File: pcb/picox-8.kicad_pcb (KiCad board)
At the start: 2 copper layers, 287.5 x 119 mm, 86 parts, among them J1 PX-8 Expansion Port, U1 XC95144XL-TQ100

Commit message: PCB work
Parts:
- added J2: Mini-DIN-8, Connector_DIN:minidin-8, F.Cu at (247.7, 96.0)
- added J3: SD_Card, Connector_Card:SD_TE_2041021, F.Cu at (286.5, 102.5)
- added SW1: SW_Push, Button_Switch_THT:SW_Tactile_SPST_Angled_PTS645Vx39-2LFS, F.Cu at (260.2, 92.0)
- added U2: MAX3232, Package_SO:SOP-16_3.9x9.9mm_P1.27mm, F.Cu at (229.3, 112.0)
- added U3: Pico_W, RPI PIco:RPi_Pico_SMD_TH, F.Cu at (205.1, 175.1)
- added U4: AZ1117-3.3, Package_TO_SOT_SMD:SOT-223, F.Cu at (232.3, 163.2)
- moved R4 64.1 mm to (122.0, 117.7)
- moved R1 62.6 mm to (123.6, 114.2)
- moved R10 62.6 mm to (128.1, 117.7)
- moved R12 62.6 mm to (129.6, 117.7)
- moved R13 62.6 mm to (131.2, 114.2)
- moved R14 62.6 mm to (131.2, 117.7)
- moved R15 62.6 mm to (132.7, 114.2)
- moved R17 62.6 mm to (134.2, 114.2)
- moved R18 62.6 mm to (134.2, 117.7)
- moved R19 62.6 mm to (135.7, 114.2)
- moved R20 62.6 mm to (135.7, 117.7)
- moved R21 62.6 mm to (137.3, 114.2)
- moved R23 62.6 mm to (138.8, 114.2)
- moved R25 62.6 mm to (140.3, 114.2)
- moved R27 62.6 mm to (141.8, 114.2)
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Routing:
- net /A11: track 64.7 -> 0.00 mm
- net /A13: track 63.2 -> 0.00 mm
- net GND: track 0.00 -> 62.8 mm, vias 0 -> 42
- net /A12: track 62.4 -> 0.00 mm
- net /A2: track 61.7 -> 0.00 mm
- net /A14: track 60.9 -> 0.00 mm
- net /A0: track 60.3 -> 0.00 mm
- net /A1: track 59.4 -> 0.00 mm
- net /A3: track 58.7 -> 0.00 mm
- net /A15: track 57.9 -> 0.00 mm
- net /A4: track 56.5 -> 0.00 mm
- net /A5: track 56.1 -> 0.00 mm
- net /A6: track 54.4 -> 0.00 mm
- net /A7: track 53.3 -> 0.00 mm
- net /A10: track 51.5 -> 0.00 mm
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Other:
- outline, holes or cut-outs redrawn

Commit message: pcb work
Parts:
- removed U4: AZ1117-3.3, Package_TO_SOT_SMD:SOT-223
- added C1: 100nF, Capacitor_SMD:C_0603_1608Metric_Pad1.08x0.95mm_HandSolder, B.Cu at (158.4, 143.1)
- added C2: 100nF, Capacitor_SMD:C_0603_1608Metric_Pad1.08x0.95mm_HandSolder, B.Cu at (161.4, 143.1)
- added C3: 100nF, Capacitor_SMD:C_0603_1608Metric_Pad1.08x0.95mm_HandSolder, B.Cu at (160.4, 148.3)
- added C4: 100nF, Capacitor_SMD:C_0603_1608Metric_Pad1.08x0.95mm_HandSolder, B.Cu at (160.4, 154.4)
- added C5: 100nF, Capacitor_SMD:C_0603_1608Metric_Pad1.08x0.95mm_HandSolder, B.Cu at (150.1, 148.3)
- added C6: 100nF, Capacitor_SMD:C_0603_1608Metric_Pad1.08x0.95mm_HandSolder, B.Cu at (150.4, 153.3)
- added C7: 100nF, Capacitor_SMD:C_0603_1608Metric_Pad1.08x0.95mm_HandSolder, B.Cu at (151.4, 158.6)
- added J4: USB_C_Receptacle_USB2.0, Connector_USB:USB_C_Receptacle_G-Switch_GT-USB-7010ASV, F.Cu at (326.6, 93.1)
- added J5: CONN_CPLD_JTAG, Connector_IDC:IDC-Header_2x05_P2.54mm_Vertical, F.Cu at (95.6, 118.7)
- added Q1: Q_PMOS_DGS, Package_TO_SOT_SMD:SOT-23-3, F.Cu at (234.5, 124.4)
- added U5: MCP73871-2CC, Package_DFN_QFN:QFN-20-1EP_4x4mm_P0.5mm_EP2.5x2.5mm, F.Cu at (246.3, 177.3)
- J3: value SD_Card -> 693063010911; footprint Connector_Card:SD_TE_2041021 -> hans-kicad-footprints:Wuerth SD Card 693063010911
- moved U3 30.2 mm to (216.3, 147.0)
- moved U2 18.6 mm to (247.9, 111.6), turned to 90 degrees
- moved J3 3.58 mm to (283.0, 102.1)
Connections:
- J2 pad 10: (no net) -> unconnected-(J2-SHIELD-Pad10)
- J2 pad 11: (no net) -> unconnected-(J2-SHIELD-Pad11)
- J2 pad 9: (no net) -> unconnected-(J2-SHIELD-Pad9)
- J3 pad 1: unconnected-(J3-CD/DAT3-Pad1) -> /SD_CS
- J3 pad 10: unconnected-(J3-CARD_DETECT-Pad10) -> /SD_CD
- J3 pad 11: unconnected-(J3-WRITE_PROTECT-Pad11) -> /SD_WP
- J3 pad 2: unconnected-(J3-CMD-Pad2) -> /SD_MOSI
- J3 pad 3: unconnected-(J3-VSS-Pad3) -> GND
- J3 pad 4: unconnected-(J3-VDD-Pad4) -> +3.3V
- J3 pad 5: unconnected-(J3-CLK-Pad5) -> /SD_CLK
- J3 pad 6: unconnected-(J3-VSS-Pad6) -> GND
- J3 pad 7: unconnected-(J3-DAT0-Pad7) -> /SD_MISO
- SW1 pad 1: unconnected-(SW1-Pad1) -> /BTN_FAILSAFE
- SW1 pad 2: unconnected-(SW1-Pad2) -> GND
- U1 pad 100: unconnected-(U1-GND-Pad100) -> GND
- U1 pad 21: unconnected-(U1-GND-Pad21) -> GND
- U1 pad 26: unconnected-(U1-VCCIO-Pad26) -> +3.3V
- U1 pad 31: unconnected-(U1-GND-Pad31) -> GND
- U1 pad 38: unconnected-(U1-VCCIO-Pad38) -> +3.3V
- U1 pad 44: unconnected-(U1-GND-Pad44) -> GND
- U1 pad 45: unconnected-(U1-TDI-Pad45) -> Net-(J5-TDI)
- U1 pad 47: unconnected-(U1-TMS-Pad47) -> Net-(J5-TMS)
- U1 pad 48: unconnected-(U1-TCK-Pad48) -> Net-(J5-TCK)
- U1 pad 5: unconnected-(U1-VCCINT-Pad5) -> +3.3V
- U1 pad 51: unconnected-(U1-VCCIO-Pad51) -> +3.3V
- U1 pad 57: unconnected-(U1-VCCINT-Pad57) -> +3.3V
- U1 pad 62: unconnected-(U1-GND-Pad62) -> GND
- U1 pad 69: unconnected-(U1-GND-Pad69) -> GND
- U1 pad 75: unconnected-(U1-GND-Pad75) -> GND
- U1 pad 83: unconnected-(U1-TDO-Pad83) -> Net-(J5-TDO)
- U1 pad 84: unconnected-(U1-GND-Pad84) -> GND
- U1 pad 88: unconnected-(U1-VCCIO-Pad88) -> +3.3V
- U1 pad 98: unconnected-(U1-VCCINT-Pad98) -> +3.3V
- U3 pad 21: unconnected-(U3-GPIO16-Pad21) -> /SD_MISO
- U3 pad 22: unconnected-(U3-GPIO17-Pad22) -> /SD_CS
- U3 pad 24: unconnected-(U3-GPIO18-Pad24) -> /SD_CLK
- U3 pad 25: unconnected-(U3-GPIO19-Pad25) -> /SD_MOSI
- U3 pad 26: unconnected-(U3-GPIO20-Pad26) -> /SD_CD
- U3 pad 27: unconnected-(U3-GPIO21-Pad27) -> /SD_WP
- U3 pad 29: unconnected-(U3-GPIO22-Pad29) -> /BTN_FAILSAFE
- U3 pad 39: unconnected-(U3-VSYS-Pad39) -> /VSYS
- U3 pad 40: unconnected-(U3-VBUS-Pad40) -> /VBUS
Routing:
- net +3.3V: track 0.00 -> 11.7 mm, vias 0 -> 7
- added copper zone on B.Cu, net GND
- added copper zone on F.Cu, net GND

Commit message: cpld & pcb work
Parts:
- added C10: 100nF, Capacitor_SMD:C_0603_1608Metric_Pad1.08x0.95mm_HandSolder, F.Cu at (253.2, 113.5)
- added C11: 100nF, Capacitor_SMD:C_0603_1608Metric_Pad1.08x0.95mm_HandSolder, F.Cu at (253.2, 109.0)
- added C12: 100nF, Capacitor_SMD:C_0603_1608Metric_Pad1.08x0.95mm_HandSolder, F.Cu at (241.7, 113.3)
- added C8: 100nF, Capacitor_SMD:C_0603_1608Metric_Pad1.08x0.95mm_HandSolder, F.Cu at (253.2, 112.0)
- added C9: 100nF, Capacitor_SMD:C_0603_1608Metric_Pad1.08x0.95mm_HandSolder, F.Cu at (253.2, 110.5)
- added R85: 10k, Resistor_SMD:R_0603_1608Metric_Pad0.98x0.95mm_HandSolder, F.Cu at (231.4, 139.0)
- added R86: 10k, Resistor_SMD:R_0603_1608Metric_Pad0.98x0.95mm_HandSolder, F.Cu at (231.4, 142.5)
- added SW2: RESET, Button_Switch_THT:SW_Tactile_SPST_Angled_PTS645Vx39-2LFS, F.Cu at (317.6, 92.0)
- J2: value Mini-DIN-8 -> SERIAL
- SW1: value SW_Push -> FAILSAFE
- U2: value MAX3232 -> MAX3222; footprint Package_SO:SOP-16_3.9x9.9mm_P1.27mm -> Package_SO:TSSOP-20_4.4x5mm_P0.5mm
- U3: footprint RPI PIco:RPi_Pico_SMD_TH -> RPI PIco:RPI Pico W USB and Prog
- moved J4 50.4 mm to (276.2, 93.1)
- moved J3 16.7 mm to (299.7, 102.3)
- moved Q1 2.64 mm to (231.9, 124.4)
- moved U2 0.41 mm to (247.4, 111.6), turned to 180 degrees
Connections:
- net /VSYS renamed /PICO_VSYS
- J2 pad 1: unconnected-(J2-Pad1) -> GND
- J2 pad 10: unconnected-(J2-SHIELD-Pad10) -> GND
- J2 pad 11: unconnected-(J2-SHIELD-Pad11) -> GND
- J2 pad 2: unconnected-(J2-Pad2) -> Net-(U2-R1IN)
- J2 pad 3: unconnected-(J2-Pad3) -> Net-(U2-T1OUT)
- J2 pad 6: unconnected-(J2-Pad6) -> Net-(U2-T2OUT)
- J2 pad 7: unconnected-(J2-Pad7) -> Net-(U2-R2IN)
- J2 pad 9: unconnected-(J2-SHIELD-Pad9) -> GND
- J4 pad A1: Net-(J4-GND-PadA1) -> GND
- J4 pad A12: Net-(J4-GND-PadA1) -> GND
- J4 pad A4: Net-(J4-VBUS-PadA4) -> /VBUS
- J4 pad A9: Net-(J4-VBUS-PadA4) -> /VBUS
- J4 pad B1: Net-(J4-GND-PadA1) -> GND
- J4 pad B12: Net-(J4-GND-PadA1) -> GND
- J4 pad B4: Net-(J4-VBUS-PadA4) -> /VBUS
- J4 pad B9: Net-(J4-VBUS-PadA4) -> /VBUS
- J4 pad S1: unconnected-(J4-SHIELD-PadS1) -> GND
- Q1 pad 1: Net-(Q1-D) -> /VB1
- Q1 pad 2: /VBUS -> /PICO_VBUS
- U1 pad 10: unconnected-(U1-P10-Pad10) -> /SER_HSOUT
- U1 pad 11: unconnected-(U1-P11-Pad11) -> /SER_HSIN
- U1 pad 12: unconnected-(U1-P12-Pad12) -> /PICO_A2
- U1 pad 13: unconnected-(U1-P13-Pad13) -> /PICO_A1
- U1 pad 14: unconnected-(U1-P14-Pad14) -> /PICO_A0
- U1 pad 15: unconnected-(U1-P15-Pad15) -> /PICO_STB
- U1 pad 16: unconnected-(U1-P16-Pad16) -> /PICO_DIR
- U1 pad 17: unconnected-(U1-P17-Pad17) -> /PICO_CLK
- U1 pad 18: unconnected-(U1-P18-Pad18) -> /PICO_D7
- U1 pad 19: unconnected-(U1-P19-Pad19) -> /PICO_D6
- U1 pad 20: unconnected-(U1-P20-Pad20) -> /PICO_D5
- U1 pad 24: unconnected-(U1-P24-Pad24) -> /PICO_D4
- U1 pad 25: unconnected-(U1-P25-Pad25) -> /PICO_D3
- U1 pad 28: unconnected-(U1-P28-Pad28) -> /PICO_D2
- U1 pad 29: unconnected-(U1-P29-Pad29) -> /PICO_D1
- U1 pad 30: unconnected-(U1-P30-Pad30) -> /PICO_D0
- U1 pad 32: unconnected-(U1-P32-Pad32) -> /PICO_RXD0
- U1 pad 33: unconnected-(U1-P33-Pad33) -> /PICO_TXD0
- U1 pad 8: unconnected-(U1-P8-Pad8) -> /~{SER_EN}
- U1 pad 87: unconnected-(U1-P87-Pad87) -> /SD_WP
- U1 pad 89: unconnected-(U1-P89-Pad89) -> /SD_CD
- U1 pad 9: unconnected-(U1-P9-Pad9) -> /~{SER_SHDN}
- U1 pad 90: unconnected-(U1-P90-Pad90) -> /BTN_FAILSAFE
- U1 pad 91: unconnected-(U1-P91-Pad91) -> /BTN_RESET
- U2 pad 1: unconnected-(U2-C1+-Pad1) -> /~{SER_EN}
- U2 pad 10: unconnected-(U2-T2IN-Pad10) -> /SER_HSIN
- U2 pad 12: unconnected-(U2-R1OUT-Pad12) -> /SER_HSOUT
- U2 pad 13: unconnected-(U2-R1IN-Pad13) -> /PICO_TXD1
- U2 pad 15: unconnected-(U2-GND-Pad15) -> /PICO_RXD1
- U2 pad 16: unconnected-(U2-VCC-Pad16) -> Net-(U2-R1IN)
- U2 pad 2: unconnected-(U2-VS+-Pad2) -> Net-(U2-C1+)
- U2 pad 3: unconnected-(U2-C1--Pad3) -> Net-(U2-VS+)
- U2 pad 4: unconnected-(U2-C2+-Pad4) -> Net-(U2-C1-)
- U2 pad 5: unconnected-(U2-C2--Pad5) -> Net-(U2-C2+)
- U2 pad 6: unconnected-(U2-VS--Pad6) -> Net-(U2-C2-)
- U2 pad 7: unconnected-(U2-T2OUT-Pad7) -> Net-(U2-VS-)
- U2 pad 8: unconnected-(U2-R2IN-Pad8) -> Net-(U2-T2OUT)
- U2 pad 9: unconnected-(U2-R2OUT-Pad9) -> Net-(U2-R2IN)
- U3 pad 1: unconnected-(U3-GPIO0-Pad1) -> /PICO_TXD0
- U3 pad 10: unconnected-(U3-GPIO7-Pad10) -> /PICO_D5
- U3 pad 11: unconnected-(U3-GPIO8-Pad11) -> /PICO_D6
- U3 pad 12: unconnected-(U3-GPIO9-Pad12) -> /PICO_D7
- U3 pad 13: unconnected-(U3-GND-Pad13) -> GND
- U3 pad 14: unconnected-(U3-GPIO10-Pad14) -> /PICO_CLK
- U3 pad 15: unconnected-(U3-GPIO11-Pad15) -> /PICO_DIR
- U3 pad 16: unconnected-(U3-GPIO12-Pad16) -> /PICO_STB
- U3 pad 17: unconnected-(U3-GPIO13-Pad17) -> /PICO_A0
- U3 pad 18: unconnected-(U3-GND-Pad18) -> GND
- U3 pad 19: unconnected-(U3-GPIO14-Pad19) -> /PICO_A1
- U3 pad 2: unconnected-(U3-GPIO1-Pad2) -> /PICO_RXD0
- U3 pad 20: unconnected-(U3-GPIO15-Pad20) -> /PICO_A2
- U3 pad 23: unconnected-(U3-GND-Pad23) -> GND
- U3 pad 26: /SD_CD -> /PICO_TXD1
- U3 pad 27: /SD_WP -> /PICO_RXD1
- U3 pad 28: unconnected-(U3-GND-Pad28) -> GND
- U3 pad 29: /BTN_FAILSAFE -> unconnected-(U3-GPIO22-Pad29)
- U3 pad 3: unconnected-(U3-GND-Pad3) -> GND
- U3 pad 33: unconnected-(U3-AGND-Pad33) -> GND
- U3 pad 34: unconnected-(U3-GPIO28_ADC2-Pad34) -> Net-(U3-GPIO28_ADC2)
- U3 pad 35: unconnected-(U3-ADC_VREF-Pad35) -> +3.3V
- U3 pad 36: unconnected-(U3-3V3-Pad36) -> +3.3V
- U3 pad 38: unconnected-(U3-GND-Pad38) -> GND
- U3 pad 4: unconnected-(U3-GPIO2-Pad4) -> /PICO_D0
- U3 pad 40: /VBUS -> /PICO_VBUS
- U3 pad 5: unconnected-(U3-GPIO3-Pad5) -> /PICO_D1
- U3 pad 6: unconnected-(U3-GPIO4-Pad6) -> /PICO_D2
- U3 pad 7: unconnected-(U3-GPIO5-Pad7) -> /PICO_D3
- U3 pad 8: unconnected-(U3-GND-Pad8) -> GND
- U3 pad 9: unconnected-(U3-GPIO6-Pad9) -> /PICO_D4
- U3 pad TP1: GND -> unconnected-(U3-USB_GND-PadTP1)
- U3 pad TP2: /USB_D- -> GND
- U3 pad TP3: /USB_D+ -> /USB_D-
- U5 pad 1: Net-(Q1-D) -> /VB1
- U5 pad 2: unconnected-(U5-VPCC-Pad2) -> /VBUS
- U5 pad 20: Net-(Q1-D) -> /VB1
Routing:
- net Net-(U2-T1OUT): track 0.00 -> 17.4 mm, vias 0 -> 1
- net Net-(U2-T2OUT): track 0.00 -> 14.4 mm, vias 0 -> 1
- net Net-(U2-R2IN): track 0.00 -> 14.3 mm
- net Net-(U2-R1IN): track 0.00 -> 12.4 mm
- net /PICO_VBUS: track 0.00 -> 8.02 mm
- net Net-(U3-GPIO28_ADC2): track 0.00 -> 6.18 mm
- net /PICO_VSYS: track 0.00 -> 6.00 mm
- net Net-(U2-C1+): track 0.00 -> 5.84 mm
- net Net-(U2-C2+): track 0.00 -> 4.35 mm
- net Net-(U2-VS-): track 0.00 -> 3.14 mm
- net Net-(U2-C2-): track 0.00 -> 2.42 mm
- net Net-(U2-VS+): track 0.00 -> 2.36 mm
- net Net-(U2-C1-): track 0.00 -> 2.20 mm
- net +3.3V: track 11.7 -> 13.8 mm
- net /SPI: track 0.00 -> 1.63 mm

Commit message: schematic nearing completion
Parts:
- added C13: 10μF, Capacitor_SMD:C_0603_1608Metric_Pad1.08x0.95mm_HandSolder, F.Cu at (261.0, 169.5)
- added C14: 4.7μF, Capacitor_SMD:C_0603_1608Metric_Pad1.08x0.95mm_HandSolder, F.Cu at (261.0, 172.0)
- added C15: 4.7μF, Capacitor_SMD:C_0603_1608Metric_Pad1.08x0.95mm_HandSolder, F.Cu at (261.0, 174.6)
- added J6: NTC, Connector_PinHeader_2.54mm:PinHeader_1x02_P2.54mm_Vertical, F.Cu at (247.8, 123.6)
- added J7: BAT, Connector_JST:JST_EH_S2B-EH_1x02_P2.50mm_Horizontal, F.Cu at (277.1, 167.1)
- added R87: 10k, Resistor_SMD:R_0603_1608Metric_Pad0.98x0.95mm_HandSolder, F.Cu at (261.0, 177.1)
- added R88: 10k, Resistor_SMD:R_0603_1608Metric_Pad0.98x0.95mm_HandSolder, F.Cu at (261.0, 179.6)
- added R89: 0, Resistor_SMD:R_0603_1608Metric_Pad0.98x0.95mm_HandSolder, F.Cu at (261.0, 182.1)
- added R90: DNP, Resistor_SMD:R_0603_1608Metric_Pad0.98x0.95mm_HandSolder, F.Cu at (261.0, 184.6)
- added R91: 1k, Resistor_SMD:R_0603_1608Metric_Pad0.98x0.95mm_HandSolder, F.Cu at (261.0, 187.1)
- added R92: 10k, Resistor_SMD:R_0603_1608Metric_Pad0.98x0.95mm_HandSolder, F.Cu at (261.0, 189.6)
- moved U5 32.0 mm to (278.3, 175.3), turned to 90 degrees
- moved Q1 22.8 mm to (213.9, 138.4)
- moved R85 22.8 mm to (213.4, 153.0)
- moved R86 22.8 mm to (213.4, 156.5)
- moved U3 22.8 mm to (198.4, 161.0)
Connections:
- U1 pad 1: unconnected-(U1-I/O/GTS3-Pad1) -> /CHG_~{TE}
- U1 pad 2: unconnected-(U1-I/O/GTS4-Pad2) -> /CHG_CE
- U1 pad 92: unconnected-(U1-P92-Pad92) -> /PICO_RESET
- U1 pad 93: unconnected-(U1-P93-Pad93) -> /PICO_BOOTSEL
- U1 pad 94: unconnected-(U1-P94-Pad94) -> /CHG_STAT1
- U1 pad 95: unconnected-(U1-P95-Pad95) -> /CHG_STAT2
- U1 pad 96: unconnected-(U1-P96-Pad96) -> /CHG_~{PG}
- U1 pad 97: unconnected-(U1-P97-Pad97) -> /CHG_SEL
- U1 pad 99: unconnected-(U1-I/O/GSR-Pad99) -> /CHG_PROG2
- U3 pad 30: unconnected-(U3-RUN-Pad30) -> /PICO_RUN
- U3 pad 31: unconnected-(U3-GPIO26_ADC0-Pad31) -> /PICO_SER_HSOUT
- U3 pad 32: unconnected-(U3-GPIO27_ADC1-Pad32) -> /PICO_SER_HSIN
- U3 pad TP1: unconnected-(U3-USB_GND-PadTP1) -> GND
- U3 pad TP2: GND -> /USB_D-
- U3 pad TP3: /USB_D- -> /USB_D+
- U3 pad TP6: /USB_D+ -> /PICO_BOOTSEL
- U5 pad 10: Net-(U5-V_{SS}-Pad10) -> GND
- U5 pad 11: Net-(U5-V_{SS}-Pad10) -> GND
- U5 pad 12: unconnected-(U5-PROG3-Pad12) -> Net-(U5-PROG3)
- U5 pad 13: unconnected-(U5-PROG1-Pad13) -> Net-(U5-PROG1)
- U5 pad 14: Net-(U5-V_{BAT}-Pad14) -> /VBAT
- U5 pad 15: Net-(U5-V_{BAT}-Pad14) -> /VBAT
- U5 pad 16: unconnected-(U5-V_{BAT_SENSE}-Pad16) -> /VBAT
- U5 pad 17: unconnected-(U5-CE-Pad17) -> /CHG_CE
- U5 pad 18: Net-(U5-IN-Pad18) -> /VBUS
- U5 pad 19: Net-(U5-IN-Pad18) -> /VBUS
- U5 pad 21: Net-(U5-V_{SS}-Pad10) -> GND
- U5 pad 3: unconnected-(U5-SEL-Pad3) -> /CHG_SEL
- U5 pad 4: unconnected-(U5-PROG2-Pad4) -> /CHG_PROG2
- U5 pad 5: unconnected-(U5-THERM-Pad5) -> Net-(U5-THERM)
- U5 pad 6: unconnected-(U5-~{PG}-Pad6) -> /CHG_~{PG}
- U5 pad 7: unconnected-(U5-STAT2-Pad7) -> /CHG_STAT2
- U5 pad 8: unconnected-(U5-STAT1/~{LBO}-Pad8) -> /CHG_STAT1
- U5 pad 9: unconnected-(U5-~{TE}-Pad9) -> /CHG_~{TE}
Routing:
- net /VBAT: track 0.00 -> 8.29 mm
- net GND: vias 42 -> 46

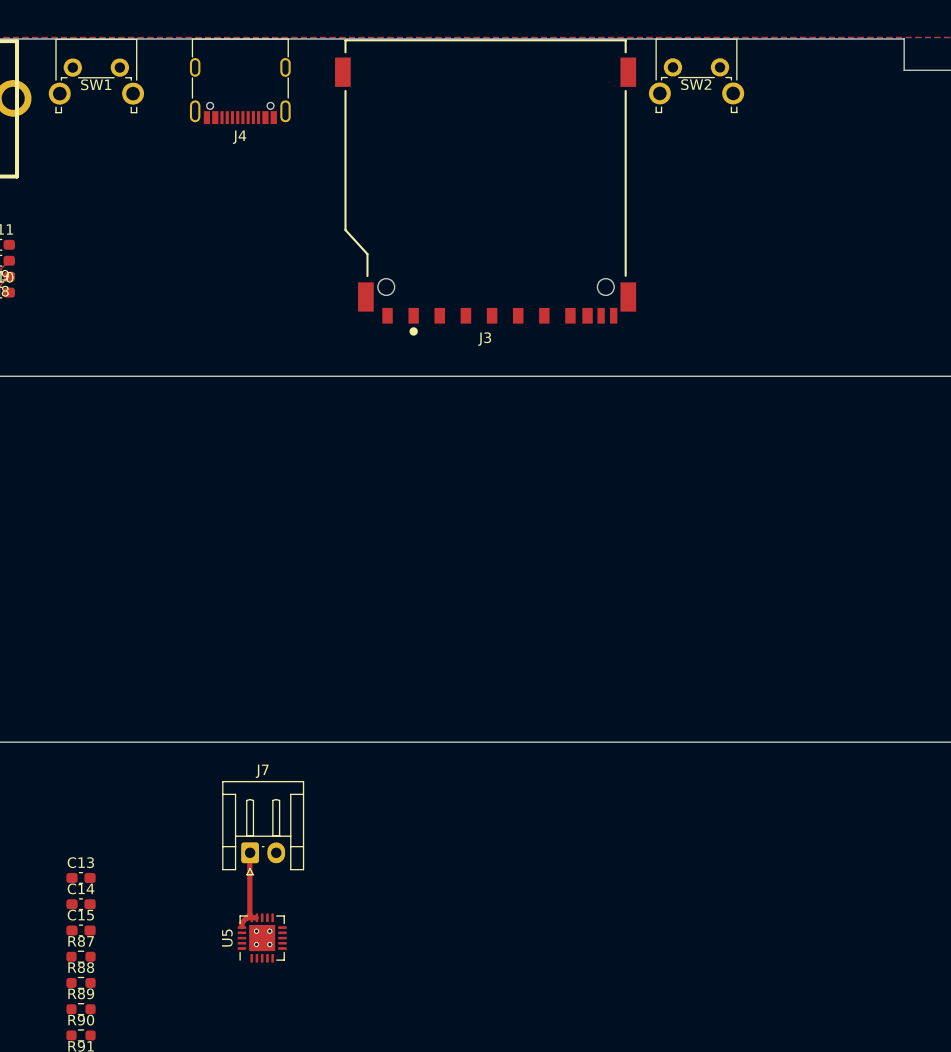
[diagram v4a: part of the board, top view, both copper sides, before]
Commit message: erc fixes
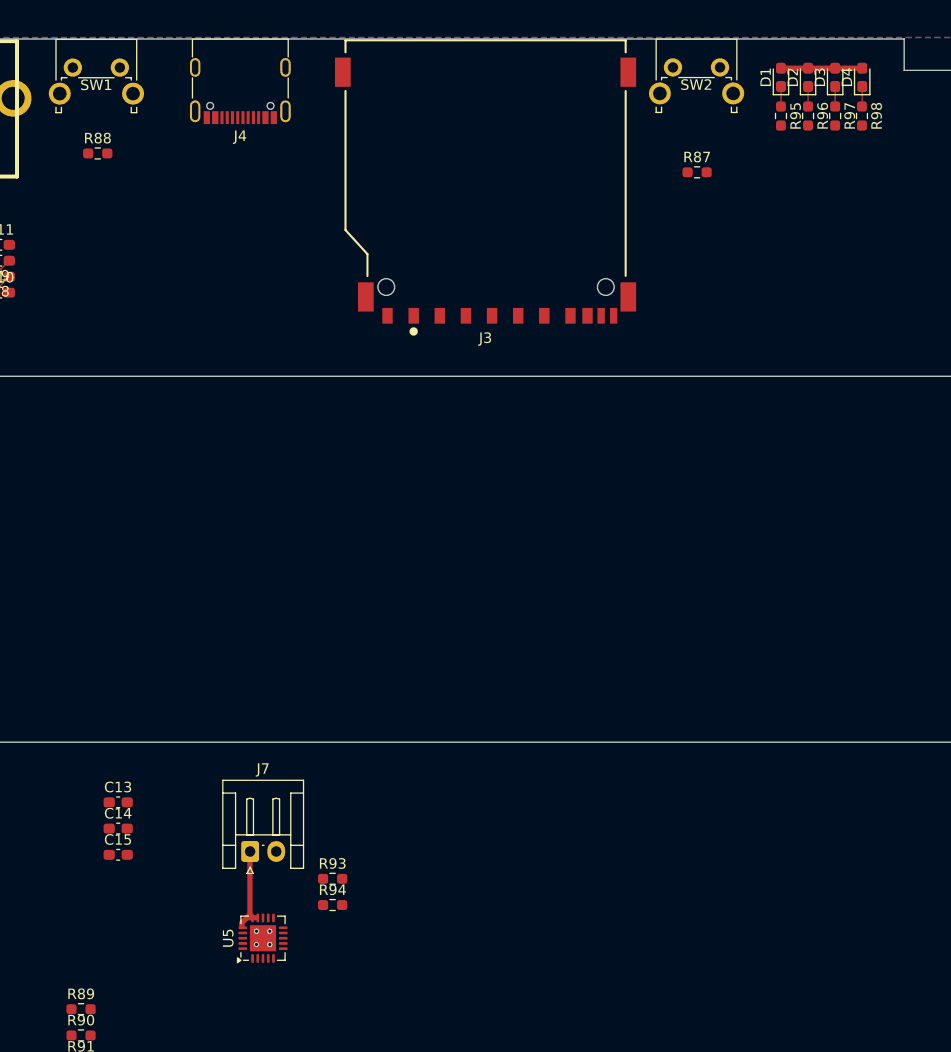
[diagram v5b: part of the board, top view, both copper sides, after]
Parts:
- added D1: LED0, LED_SMD:LED_0603_1608Metric_Pad1.05x0.95mm_HandSolder, F.Cu at (327.9, 93.0)
- added D2: LED1, LED_SMD:LED_0603_1608Metric_Pad1.05x0.95mm_HandSolder, F.Cu at (330.5, 93.0)
- added D3: LED2, LED_SMD:LED_0603_1608Metric_Pad1.05x0.95mm_HandSolder, F.Cu at (333.1, 93.0)
- added D4: LED3, LED_SMD:LED_0603_1608Metric_Pad1.05x0.95mm_HandSolder, F.Cu at (335.7, 93.0)
- added R93: 10k, Resistor_SMD:R_0603_1608Metric_Pad0.98x0.95mm_HandSolder, F.Cu at (285.0, 169.6)
- added R94: 1k, Resistor_SMD:R_0603_1608Metric_Pad0.98x0.95mm_HandSolder, F.Cu at (285.0, 172.1)
- added R95: 120, Resistor_SMD:R_0603_1608Metric_Pad0.98x0.95mm_HandSolder, F.Cu at (327.9, 96.6)
- added R96: 120, Resistor_SMD:R_0603_1608Metric_Pad0.98x0.95mm_HandSolder, F.Cu at (330.5, 96.6)
- added R97: 120, Resistor_SMD:R_0603_1608Metric_Pad0.98x0.95mm_HandSolder, F.Cu at (333.1, 96.6)
- added R98: 120, Resistor_SMD:R_0603_1608Metric_Pad0.98x0.95mm_HandSolder, F.Cu at (335.7, 96.6)
- moved R87 95.4 mm to (319.9, 102.0)
- moved R88 79.4 mm to (262.6, 100.2)
- moved C13 8.06 mm to (264.5, 162.3)
- moved C14 8.06 mm to (264.5, 164.8)
- moved C15 8.06 mm to (264.5, 167.3)
- moved J7 0.13 mm to (277.1, 167.0)
- moved U5 0.08 mm to (278.4, 175.3)
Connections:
- J4 pad A5: unconnected-(J4-CC1-PadA5) -> Net-(J4-CC1)
- J4 pad B5: unconnected-(J4-CC2-PadB5) -> Net-(J4-CC2)
- U1 pad 1: /CHG_~{TE} -> /CHG_PROG2
- U1 pad 10: /SER_HSOUT -> /~{SER_SHDN}
- U1 pad 11: /SER_HSIN -> unconnected-(U1-P11-Pad11)
- U1 pad 2: /CHG_CE -> /CHG_~{TE}
- U1 pad 3: unconnected-(U1-I/O/GTS1-Pad3) -> /CHG_CE
- U1 pad 4: unconnected-(U1-I/O/GTS2-Pad4) -> /LED0
- U1 pad 6: unconnected-(U1-P6-Pad6) -> /LED1
- U1 pad 7: unconnected-(U1-P7-Pad7) -> /LED2
- U1 pad 8: /~{SER_EN} -> /LED3
- U1 pad 9: /~{SER_SHDN} -> /~{SER_EN}
- U1 pad 92: /PICO_RESET -> unconnected-(U1-P92-Pad92)
- U1 pad 94: /CHG_STAT1 -> /PICO_RUN
- U1 pad 95: /CHG_STAT2 -> /CHG_STAT1
- U1 pad 96: /CHG_~{PG} -> /CHG_STAT2
- U1 pad 97: /CHG_SEL -> /CHG_~{PG}
- U1 pad 99: /CHG_PROG2 -> /CHG_SEL
- U2 pad 10: /SER_HSIN -> /PICO_SER_HSIN
- U2 pad 12: /SER_HSOUT -> /PICO_SER_HSOUT
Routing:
- net +3.3V: track 13.8 -> 21.6 mm
- net Net-(D4-K): track 0.00 -> 1.92 mm
- net Net-(D1-K): track 0.00 -> 1.91 mm
- net Net-(D3-K): track 0.00 -> 1.91 mm
- net Net-(D2-K): track 0.00 -> 1.91 mm

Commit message: layout work
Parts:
- moved J6 104.7 mm to (345.2, 161.9)
- moved R93 69.2 mm to (281.5, 100.5)
- moved R94 69.2 mm to (281.5, 103.0)
- moved U3 38.3 mm to (218.2, 128.3), turned to 180 degrees
- moved R86 25.8 mm to (203.1, 132.8), turned to 90 degrees
- moved R85 19.7 mm to (203.1, 136.3), turned to 90 degrees
- moved Q1 17.0 mm to (202.6, 151.0), turned to 0 degrees
- moved C12 9.92 mm to (232.6, 109.2)
- moved C10 9.92 mm to (244.2, 109.4)
- moved C11 9.92 mm to (244.2, 104.9)
- moved C8 9.92 mm to (244.2, 107.9)
- moved C9 9.92 mm to (244.2, 106.4)
- moved U2 9.92 mm to (238.4, 107.5)
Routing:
- net /BTN_RESET: track 0.00 -> 257.1 mm, vias 0 -> 3
- net /SD_WP: track 0.00 -> 253.1 mm, vias 0 -> 4
- net /SD_CD: track 0.00 -> 248.9 mm, vias 0 -> 4
- net /LED3: track 0.00 -> 246.6 mm, vias 0 -> 4
- net /LED2: track 0.00 -> 245.4 mm, vias 0 -> 4
- net /LED0: track 0.00 -> 243.7 mm, vias 0 -> 4
- net /LED1: track 0.00 -> 243.5 mm, vias 0 -> 4
- net /BTN_FAILSAFE: track 0.00 -> 201.7 mm, vias 0 -> 3
- net /~{SER_EN}: track 0.00 -> 145.9 mm, vias 0 -> 2
- net /~{SER_SHDN}: track 0.00 -> 139.8 mm, vias 0 -> 2
- net /PICO_A2: track 0.00 -> 125.1 mm, vias 0 -> 1
- net /PICO_A1: track 0.00 -> 122.3 mm, vias 0 -> 1
- net /USB_D-: track 0.00 -> 118.4 mm, vias 0 -> 3
- net /PICO_A0: track 0.00 -> 116.7 mm, vias 0 -> 1
- net /USB_D+: track 0.00 -> 114.9 mm, vias 0 -> 3
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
